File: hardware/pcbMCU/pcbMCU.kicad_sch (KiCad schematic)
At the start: 1 part

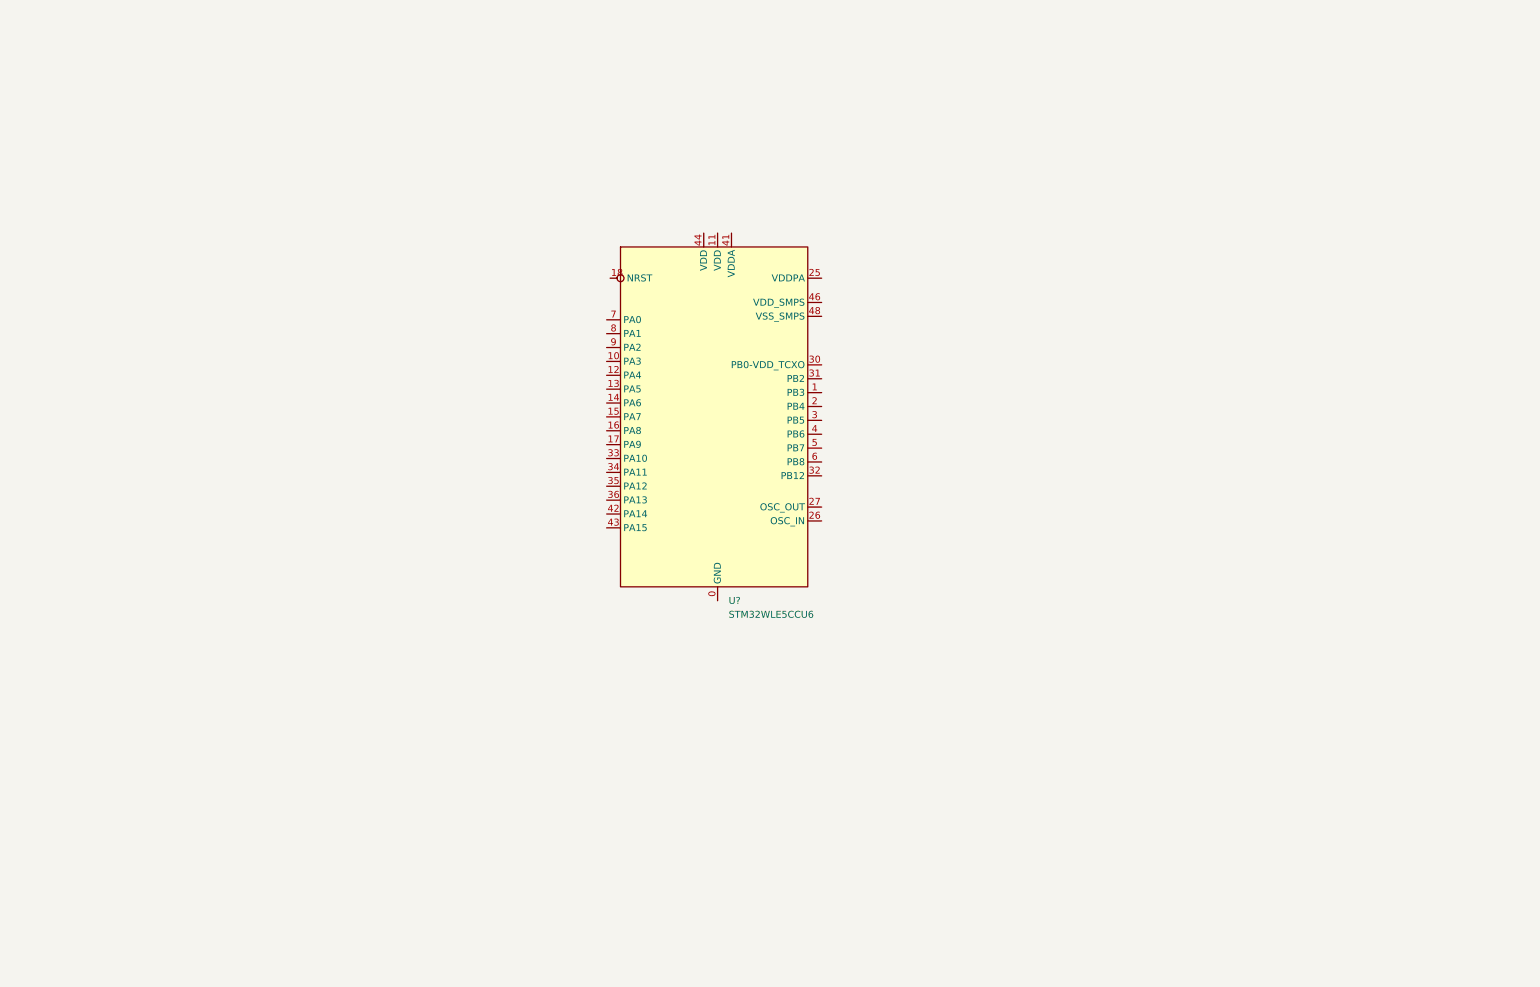
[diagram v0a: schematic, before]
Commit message: Rollback a STM32F103
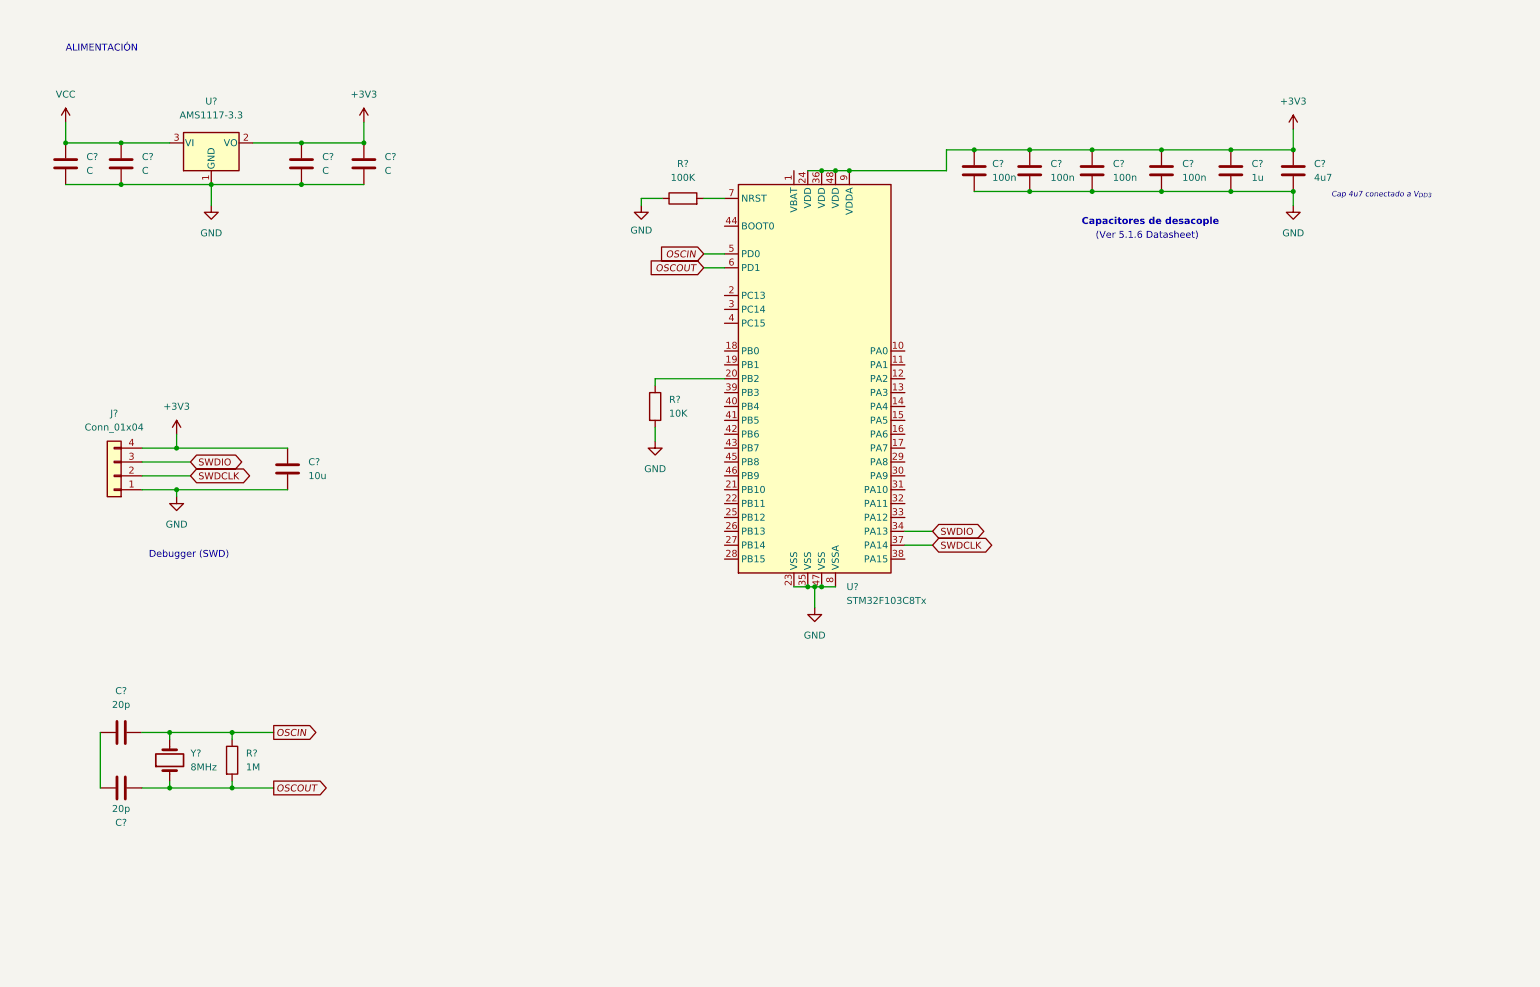
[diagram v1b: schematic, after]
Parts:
- removed U?: STM32WLE5CCU6, symbol STM32WLE5:STM32WLE5CCU6
- added C? (x2): 20p, symbol Device:C
- added C? (x4): C, symbol Device:C
- added C?: 1u, symbol Device:C
- added C? (x4): 100n, symbol Device:C
- added C?: 10u, symbol Device:C
- added C?: 4u7, symbol Device:C
- added J?: Conn_01x04, symbol Connector_Generic:Conn_01x04
- added R?: 10K, symbol Device:R
- added R?: 100K, symbol Device:R
- added R?: 1M, symbol Device:R
- added U?: STM32F103C8Tx, Package_QFP:LQFP-48_7x7mm_P0.5mm, symbol MCU_ST_STM32F1:STM32F103C8Tx
- added U?: AMS1117-3.3, Package_TO_SOT_SMD:SOT-223-3_TabPin2, symbol Regulator_Linear:AMS1117-3.3
- added Y?: 8MHz, symbol Device:Crystal
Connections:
- new net: R?.1, U?.20 (PB2)
- new net: R?.2, U?.7 (NRST)
- new net: C?.1, C?.1
- new net +3V3: C?.1, C?.1, C?.1, C?.1, C?.1, C?.1, C?.1, C?.1, C?.1, J?.4 (Pin_4), U?.2 (VO), U?.24 (VDD), U?.36 (VDD), U?.48 (VDD), U?.9 (VDDA)
- new net GND: C?.2, C?.2, C?.2, C?.2, C?.2, C?.2, C?.2, C?.2, C?.2, C?.2, C?.2, J?.1 (Pin_1), R?.1, R?.2, U?.1 (GND), U?.23 (VSS), U?.35 (VSS), U?.47 (VSS), U?.8 (VSSA)
- new net OSCIN: C?.2, R?.1, U?.5 (PD0), Y?.2
- new net OSCOUT: C?.2, R?.2, U?.6 (PD1), Y?.1
- new net SWDCLK: J?.2 (Pin_2), U?.37 (PA14)
- new net SWDIO: J?.3 (Pin_3), U?.34 (PA13)
- new net VCC: C?.1, C?.1, U?.3 (VI)
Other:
- note added: "(Ver 5.1.6 Datasheet)"
- note added: "ALIMENTACIÓN"
- note added: "Cap 4u7 conectado a V_{DD3}"
- note added: "Capacitores de desacople"
- note added: "Debugger (SWD)"

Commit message: Regulación de alimentación de entrada
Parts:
- removed C? (x2): C, symbol Device:C
- removed R?: 100K, symbol Device:R
- added C?: 100n, symbol Device:C
- added D?: D_Schottky_Small, symbol Device:D_Schottky_Small
- added F?: 500mA, symbol Device:Fuse_Small
- added FB? (x2): 100 @ 100MHz, symbol Device:FerriteBead_Small
- C? (x2): value C -> 10u
- C?: value 1u -> 10u
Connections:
- net +3V3: now also U?.1 (VBAT), FB?.1; no longer U?.9 (VDDA)
- net GND: now also C?.2
- net VCC: now also D?.2 (A); no longer C?.1, U?.3 (VI)
- net NRST: now reaches U?.7 (NRST)
- net BOOT0: now reaches U?.44 (BOOT0)
- new net: D?.1 (K), F?.1
- new net: C?.1, FB?.2, U?.3 (VI)
- new net: F?.2, FB?.1
- new net +3.3VA: C?.1, FB?.2, U?.9 (VDDA)
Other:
- note added: "Filtro para ADC"
- note added: "Protección entrada"
- note added: "REGULACION"
- note removed: "ALIMENTACIÓN"
- moved on the sheet: C?, U?

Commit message: Rev1 terminada
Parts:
- removed R?: 10K, symbol Device:R
- added H1, H2, H3, H4: MountingHole, symbol Mechanical:MountingHole
- added J1: Conn_01x02, symbol Connector_Generic:Conn_01x02
- added J3: Conn_01x03, symbol Connector_Generic:Conn_01x03
- added R1: 10K, symbol Device:R
- added SW1: SW_SPDT, symbol Switch:SW_SPDT
- added U3: Ai-Thinker-Ra-02, RF_Module:Ai-Thinker-Ra-01-LoRa, symbol RF_Module:Ai-Thinker-Ra-02
- gave numbers to parts that had none: 21
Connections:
- net +3V3: now also J3.1 (Pin_1), SW1.3 (C), U3.3 (VDD)
- net BOOT0: now also R1.1
- net GND: now also J1.1 (Pin_1), J3.2 (Pin_2), SW1.1 (A), U3.1 (GND), U3.16 (GND), U3.2 (GND), U3.9 (GND)
- net VCC: now also J1.2 (Pin_2)
- net LoRa_DIO0: now reaches U2.20 (PB2)
- net LoRa_DIO0: now also U3.5 (DIO0)
- net ADC_MIC: now reaches U2.10 (PA0)
- net ADC_MIC: now also J3.3 (Pin_3)
- net ADC_SP: now reaches U2.11 (PA1)
- net SPI1_SCK: now reaches U2.15 (PA5)
- net SPI1_SCK: now also U3.12 (SCK)
- net SPI1_MISO: now reaches U2.16 (PA6)
- net SPI1_MISO: now also U3.13 (MISO)
- net SPI1_MOSI: now reaches U2.17 (PA7)
- net SPI1_MOSI: now also U3.14 (MOSI)
- net ~{SS}: now reaches U2.18 (PB0)
- net ~{SS}: now also U3.15 (~{NSS})
- net LoRa_~{RST}: now reaches U2.19 (PB1)
- net LoRa_~{RST}: now also U3.4 (~{RESET})
- net NRST renamed ~{RST}
- new net: R1.2, SW1.2 (B)
- no-connect marks 0 -> 30
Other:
- note added: "ALIMENTACIÓN/REGULACIÓN"
- note added: "BOOT0 = 1: "Program mode" (podemos cargar firmware) BOOT0 = 0: "Run Mode" (Corre firmware)"
- note added: "CONECTORES/MONTAJE"
- note added: "DEBUGGER (SWD)"
- note added: "En caso de usar otro cristal comercial, ver si el datasheet recomienda otros capacitores de carga"
- note added: "En las notas de aplicación AN2867 de ST, aparece una tabla de fabricantes, cristales comerciales, y capacitores de carga recomendados."
- note added: "MCU"
- note added: "MICRÓFONO SONOMETRO"
- note added: "MÓDULO LORA"
- note added: "PERIFÉRICOS"
- note added: "Tendremos que ver si no es más efectivo poner una linea SPI/I2C/etc para evitar ruido, en vez de mandar directamente al ADC."
- note removed: "Debugger (SWD)"
- note removed: "REGULACION"
- company: (none) -> Franco Montanari, Dante Conti, Maximiliano Gonzales
- title: (none) -> Sensor partículas IoT
- moved on the sheet: C1, C10, C11, C12, C2, C3, C4, C5, C6, C7, C8, C9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

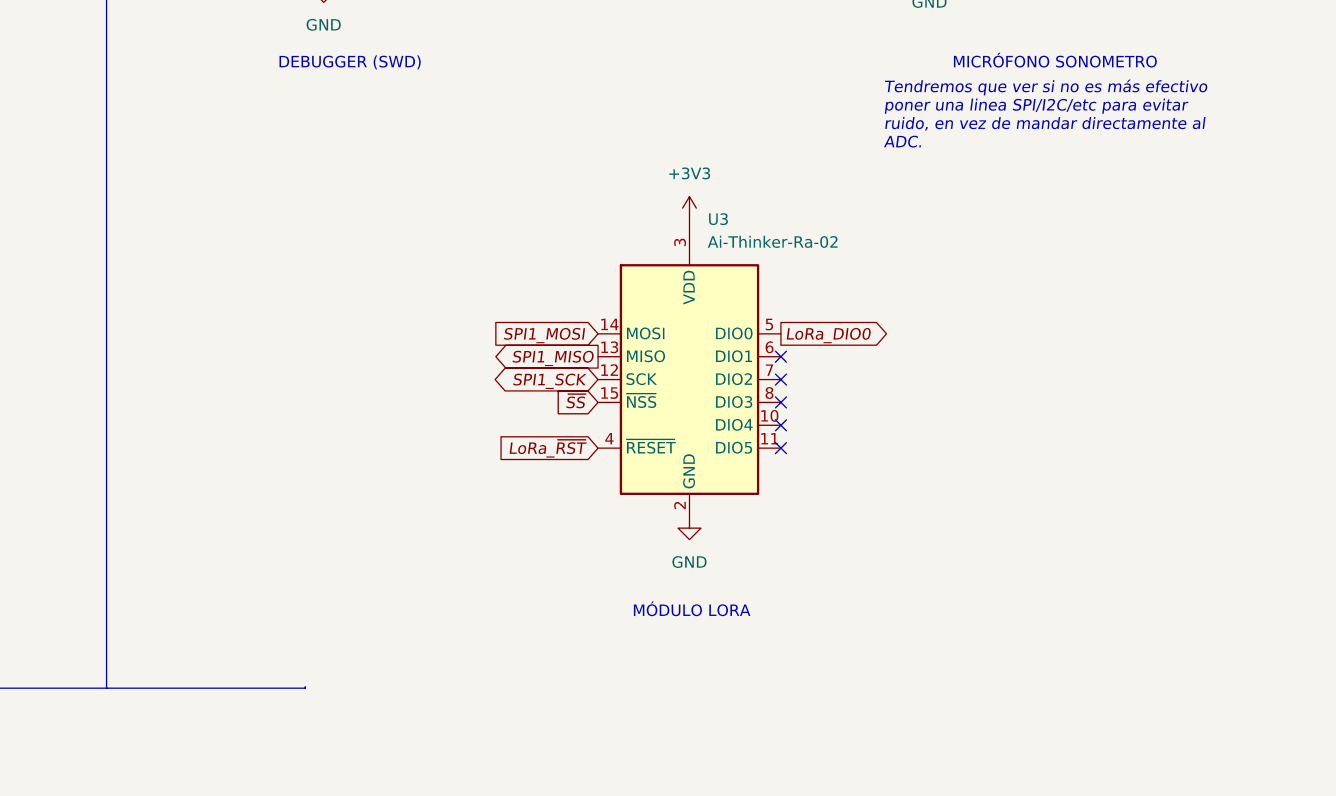
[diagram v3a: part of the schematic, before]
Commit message: Añadido medidor partículas
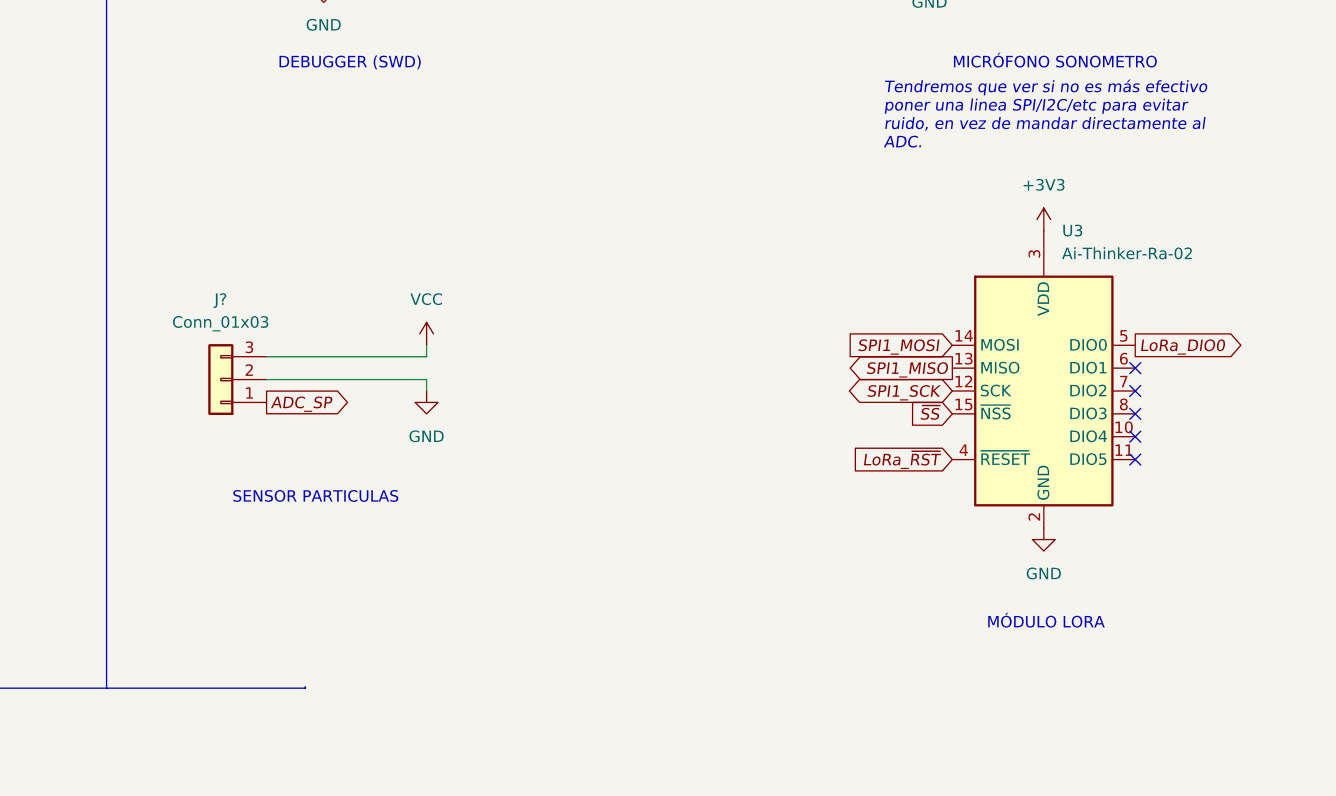
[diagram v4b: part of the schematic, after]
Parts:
- added J?: Conn_01x03, symbol Connector_Generic:Conn_01x03
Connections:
- net ADC_SP: now also J?.1 (Pin_1)
- net GND: now also J?.2 (Pin_2)
- net VCC: now also J?.3 (Pin_3)
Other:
- note added: "SENSOR PARTICULAS"
- moved on the sheet: U3
